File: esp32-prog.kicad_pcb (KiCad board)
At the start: 2 copper layers, 55 x 30 mm, 38 parts, among them J1 USB_B_Micro_10118194-0001LF, J2 1.27mm_50mils_male_DW127R-22-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, Q1 AO3400A, Q2 AO3400A, SW1 SW_DIP_x02_50mil_1.27mm_TP-02, U1 AMS1117-3.3, U2 SRV05-4, U3 CH340C, U4 74LVC1G125GW_Nexperia, U5 74LVC1G125GW_Nexperia, U6 74LVC1G125GW_Nexperia, U7 74LVC1G125GW_Nexperia

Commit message: draft route complete
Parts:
- added H1: MH, MountingHole:MountingHole_3.2mm_M3_ISO7380_Pad, F.Cu at (154.5, 52.0)
- added H2: MH, MountingHole:MountingHole_3.2mm_M3_ISO7380_Pad, F.Cu at (200.5, 52.0)
- added H3: MH, MountingHole:MountingHole_3.2mm_M3_ISO7380_Pad, F.Cu at (200.5, 73.0)
- added H4: MH, MountingHole:MountingHole_3.2mm_M3_ISO7380_Pad, F.Cu at (154.5, 73.0)
- moved R10 47.5 mm to (195.3, 61.7), turned to -90 degrees
- moved Q2 43.9 mm to (193.1, 64.6), turned to -90 degrees
- moved R12 41.6 mm to (195.3, 63.6), turned to 90 degrees
- moved J2 35.6 mm to (201.4, 65.0), turned to 180 degrees
- moved R11 32.8 mm to (190.8, 63.6), turned to 90 degrees
- moved Q1 32.0 mm to (193.1, 60.7), turned to 90 degrees
- moved R9 30.3 mm to (190.8, 61.7), turned to -90 degrees
- moved R3 8.01 mm to (187.8, 52.5)
- moved R2 8.00 mm to (187.8, 49.9)
- moved D2 7.98 mm to (190.3, 52.9)
- moved D3 7.97 mm to (190.3, 51.3)
- moved C1 7.97 mm to (160.7, 54.0)
- moved C2 7.97 mm to (174.0, 53.1)
- moved D1 7.97 mm to (190.3, 49.7)
- moved U1 7.97 mm to (166.0, 51.8)
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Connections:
- J1 pad 6: GND -> unconnected-(J1-Pad6)
- J2 pad 10: GND -> unconnected-(J2-Pad10)
- J2 pad 3: unconnected-(J2-Pad3) -> GND
- J2 pad 4: unconnected-(J2-Pad4) -> GND
- J2 pad 9: GND -> unconnected-(J2-Pad9)
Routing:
- net GND: track 1.15 -> 58.8 mm, vias 1 -> 38
- net +3.3V: track 23.9 -> 72.2 mm
- net /RXD: track 0.00 -> 38.1 mm
- net +5V: track 31.2 -> 61.5 mm
- net /ESP_EN: track 0.00 -> 17.9 mm, vias 0 -> 2
- net /TXD: track 10.5 -> 25.6 mm
- net Net-(R5-Pad1): track 13.6 -> 1.33 mm
- net unconnected-(J1-Pad6): track 0.00 -> 11.2 mm
- net +3.3VA: track 4.21 -> 15.0 mm
- net VBUS: track 48.4 -> 57.7 mm
- net /ESP_BOOT: track 0.00 -> 8.88 mm, vias 0 -> 2
- net Net-(R10-Pad1): track 10.9 -> 17.8 mm
- net Net-(Q1-Pad2): track 0.00 -> 4.01 mm
- net Net-(Q1-Pad1): track 0.00 -> 4.00 mm
- net Net-(R9-Pad1): track 10.8 -> 14.2 mm
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- added copper zone on B.Cu, net GND
- added copper zone on F.Cu, net GND
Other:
- outline, holes or cut-outs redrawn

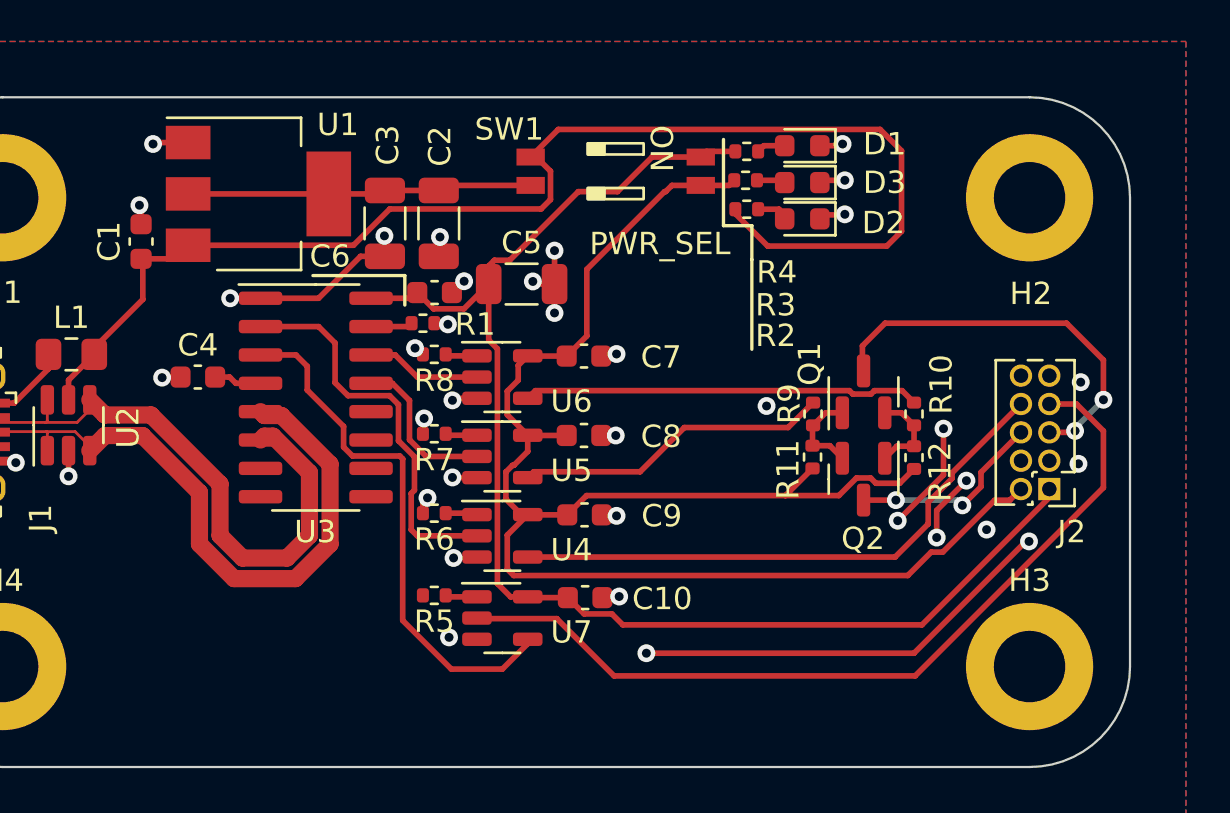
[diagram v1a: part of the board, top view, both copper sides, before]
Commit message: draft route: add more gnd guard traces
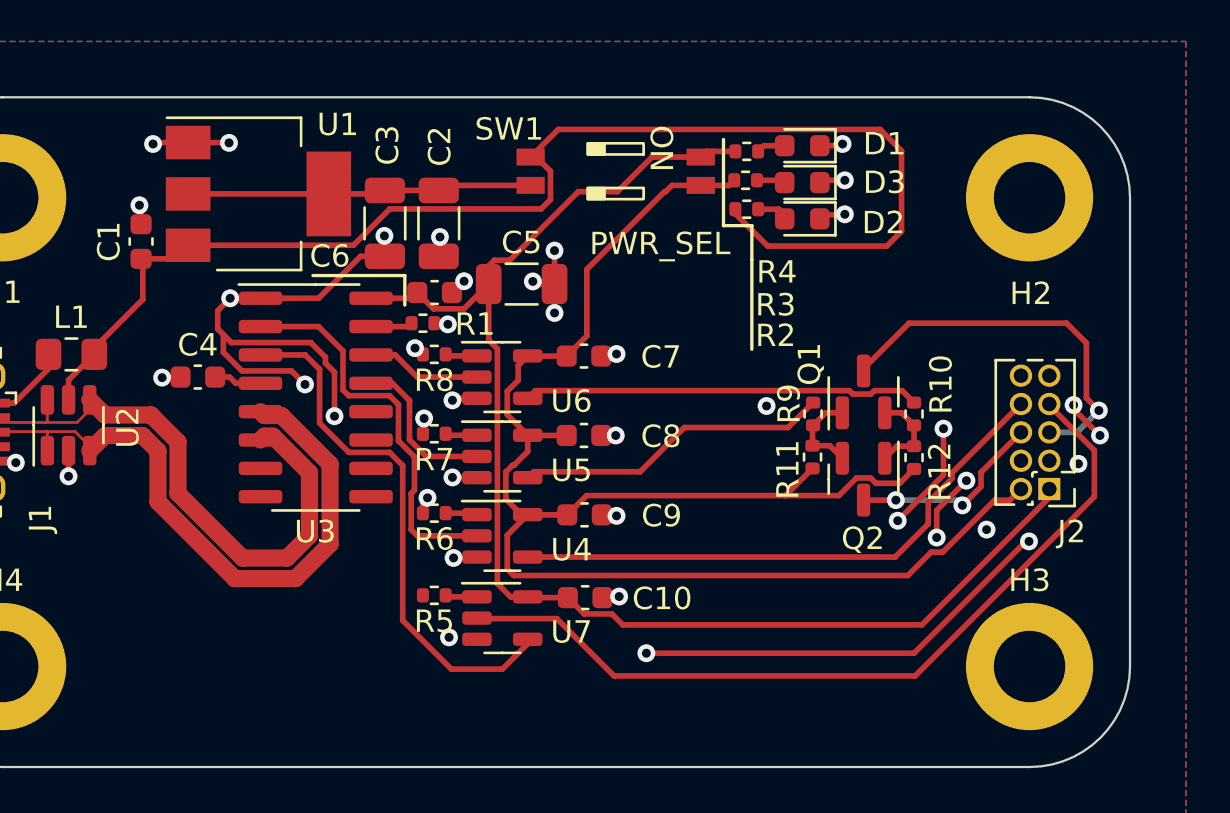
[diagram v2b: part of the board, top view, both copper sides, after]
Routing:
- net GND: track 58.8 -> 77.3 mm, vias 38 -> 42
- net /RXD: track 38.1 -> 37.0 mm
- net /ESP_EN: track 17.9 -> 17.1 mm, vias 2 -> 1

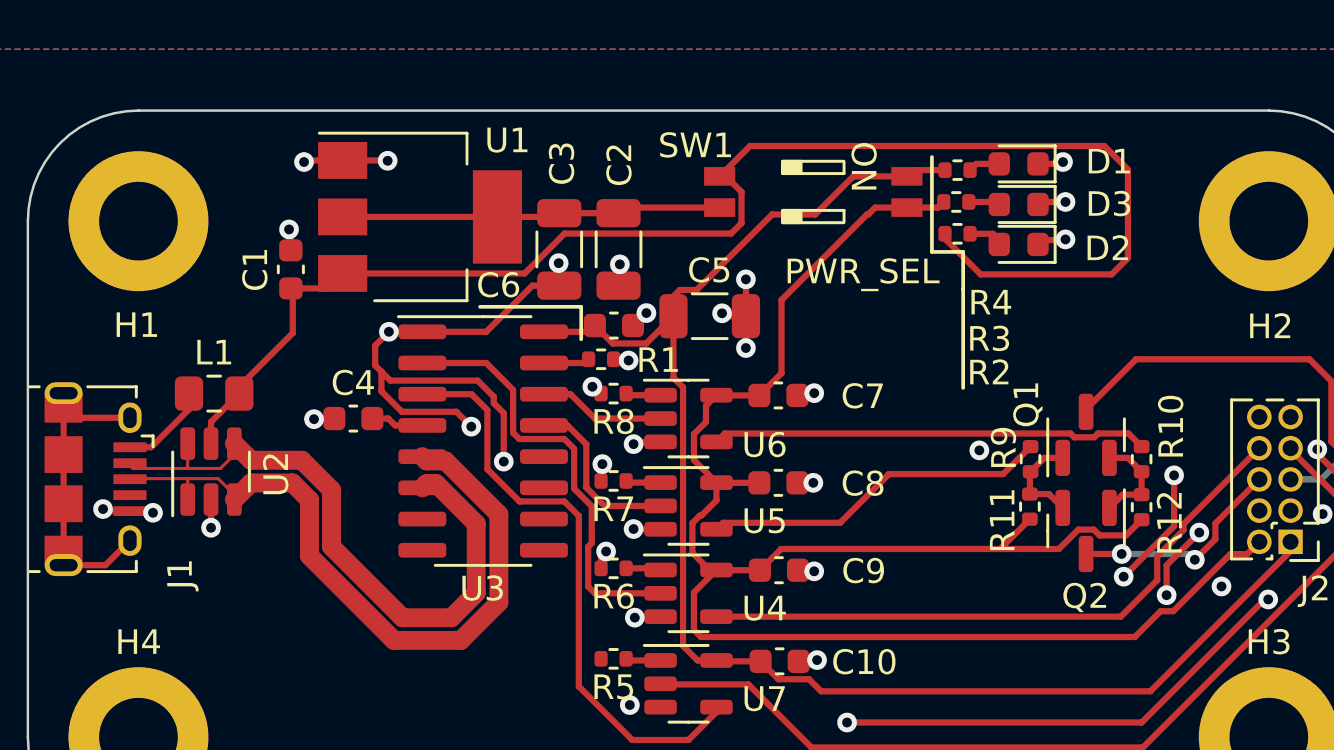
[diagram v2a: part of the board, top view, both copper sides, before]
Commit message: draft route: complete, ready for review
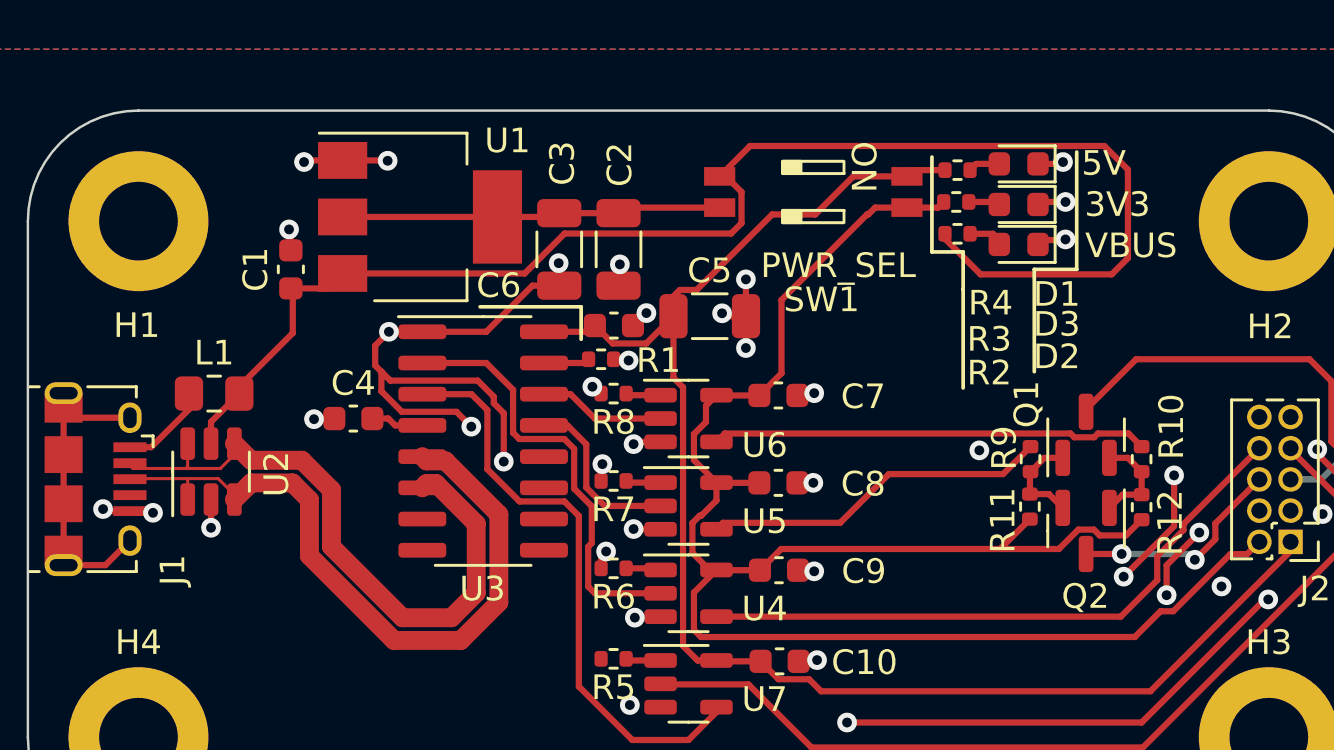
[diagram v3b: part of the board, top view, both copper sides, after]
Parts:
- J1: footprint Connector_USB:USB_Micro-B_Amphenol_10118194_Horizontal -> 00-kiml-connector-usb:USB_Micro-B_Amphenol_10118194_Horizontal
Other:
- board text added: "3V3"
- board text added: "5V"
- board text added: "VBUS"

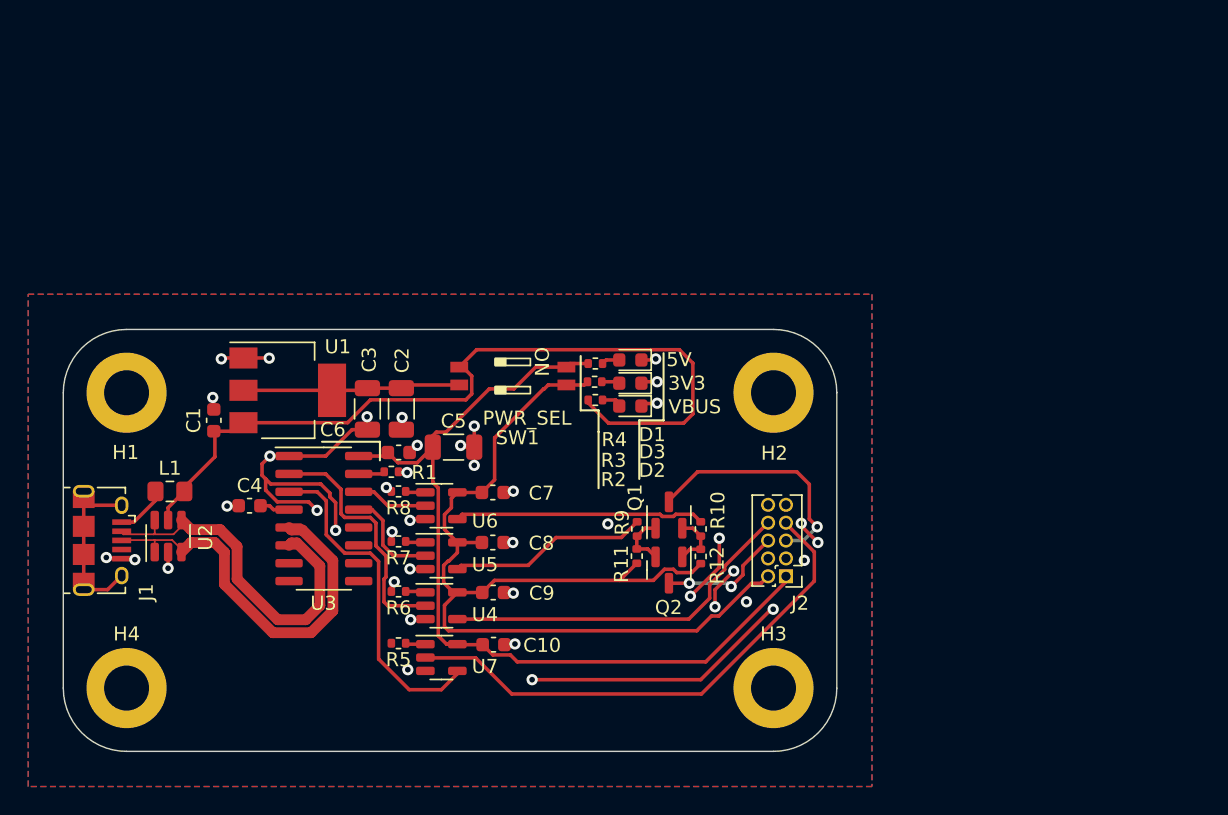
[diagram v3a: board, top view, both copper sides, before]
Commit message: route: addressed R. comments w.r.t. power assign
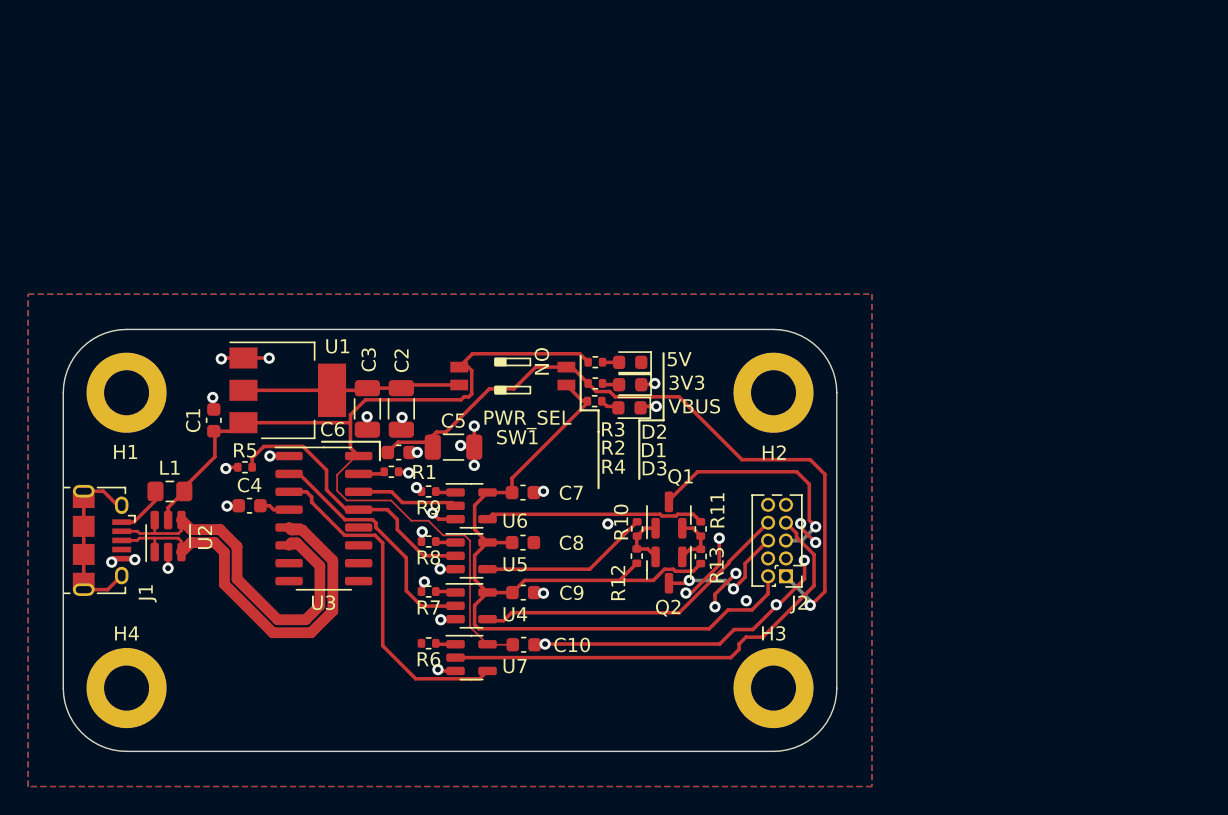
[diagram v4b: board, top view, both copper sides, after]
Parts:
- added R5: 10k_0402_0402WGF1002TCE, Resistor_SMD:R_0402_1005Metric, F.Cu at (162.9, 57.3)
- moved D2 3.11 mm to (190.3, 49.8)
- moved R3 2.68 mm to (187.8, 49.8)
- moved C10 2.14 mm to (182.7, 69.9)
- moved C7 2.14 mm to (182.7, 59.1)
- moved C8 2.14 mm to (182.7, 62.7)
- moved U4 2.14 mm to (179.0, 67.2)
- moved U5 2.14 mm to (179.0, 63.6)
- moved U6 2.14 mm to (179.0, 60.0)
- moved U7 2.14 mm to (179.0, 70.8)
- moved C9 2.14 mm to (182.7, 66.2)
- moved R6 2.14 mm to (176.0, 69.8)
- moved R7 2.14 mm to (176.0, 66.1)
- moved R8 2.14 mm to (176.0, 62.6)
- moved R9 2.14 mm to (176.0, 59.0)
- moved D1 1.76 mm to (190.3, 51.4)
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- renumbered R9 to R10, R10 to R11, R11 to R12, R12 to R13, R5 to R6, R6 to R7, R7 to R8, R8 to R9
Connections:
- C10 pad 1: +5V -> VBUS
- U3 pad 16: +5V -> VBUS
- U7 pad 5: +5V -> VBUS
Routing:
- net GND: track 77.3 -> 58.9 mm, vias 42 -> 38
- net Net-(U3-Pad13): track 7.13 -> 19.6 mm
- net +5V: track 61.5 -> 49.9 mm, vias 0 -> 1
- net VBUS: track 57.7 -> 65.1 mm
- net +3.3V: track 72.2 -> 66.6 mm
- net /RXD: track 37.0 -> 33.1 mm
- net /TXD: track 25.6 -> 22.9 mm
- net Net-(R11-Pad1): track 17.8 -> 15.6 mm
- net Net-(U3-Pad14): track 5.15 -> 7.30 mm
- net Net-(R10-Pad1): track 14.2 -> 12.0 mm
- net unconnected-(J1-Pad6): track 11.2 -> 12.0 mm
- net /UD+: track 28.7 -> 29.5 mm
- net /UD-: track 25.9 -> 26.4 mm

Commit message: route: add fancy silk
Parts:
- added G***: LOGO, 00-kiml-maxlab-logos:maxlab_logo_full_45mm, B.Cu at (176.1, 62.4)
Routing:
- net Net-(U3-Pad2): track 17.3 -> 16.5 mm
- net +5V: track 49.9 -> 49.2 mm
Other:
- board text added: "NC RX EN GND 5V"
- board text added: "NC TX BOOT GND 3V3"
- board text added: "Pinout:"
- board text added: "USB ESP32, TagConnect adapter"
- board text added: "maxlab.io"
- board text added: "rev0"
- board text added: "• • • • •"
